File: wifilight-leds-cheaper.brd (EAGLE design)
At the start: 50.8 x 50.8 mm, 57 parts

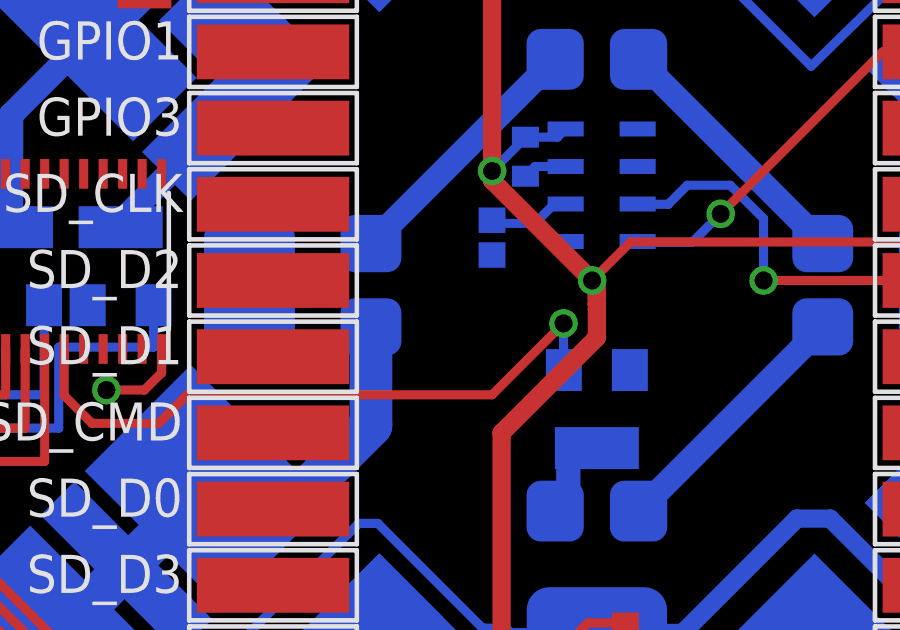
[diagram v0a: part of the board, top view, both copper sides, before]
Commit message: Damnit, how was I supposed to power this thing?
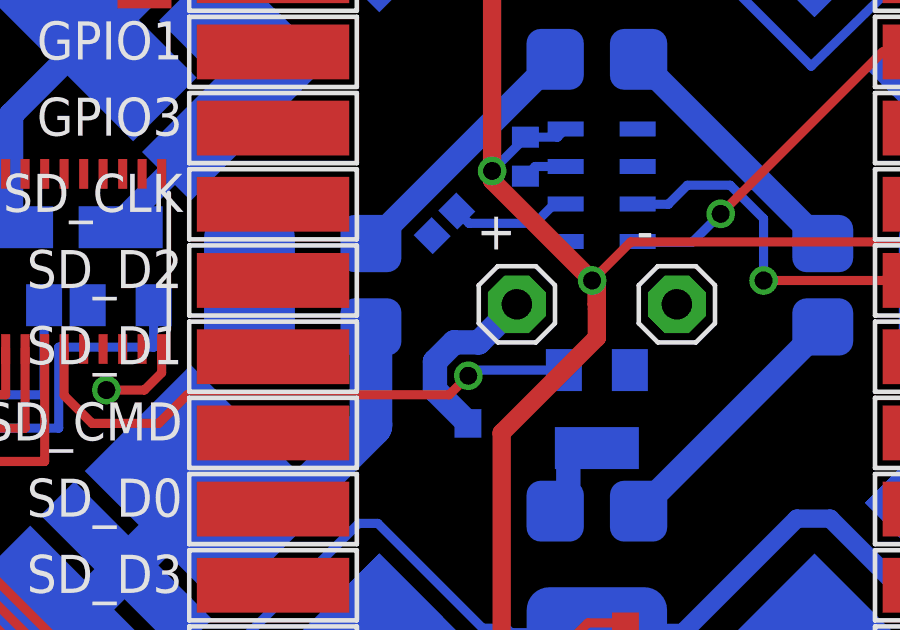
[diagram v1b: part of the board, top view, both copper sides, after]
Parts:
- added +, -: (no value), adafruit:1X01
- added D2: (no value), SparkFun-DiscreteSemi:SOD-123
- moved C4 1.66 mm to (20.3, 27.5), turned to 315 degrees
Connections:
- new net N$18: +.1, D2.A
- net 12V: now also D2.C
- net GND: now also -.1
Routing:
- net N$18: track 0.00 -> 6.04 mm
- net WHITE: track 21.5 -> 19.3 mm
- net N$17: track 2.76 -> 4.07 mm
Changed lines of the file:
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@@
 </element>
 <element name="TEMPERATURE" library="SparkFun-Sensors" package="LGA8" value="MPL3115A2LGA8" x="25.55875" y="28.73375" rot="MR180"/>
-<element name="C4" library="SparkFun-Capacitors" package="0402-CAP" value="0.1uF" x="21.9075" y="26.9875" rot="MR270">
-<attribute name="PROD_ID" value="CAP-12416" x="21.9075" y="26.9875" size="1.778" layer="28" rot="MR270" display="off"/>
+<element name="C4" library="SparkFun-Capacitors" package="0402-CAP" value="0.1uF" x="20.32" y="27.46375" rot="MR315">
+<attribute name="PROD_ID" value="CAP-12416" x="20.32" y="27.46375" size="1.778" layer="28" rot="MR315" display="off"/>
 </element>
 <element name="RESET" library="switch-omron" package="B3F-10XX" value="" x="25.4" y="45.212" rot="R270">
@@
 <element name="THINKING" library="led" package="CHIP-LED0805" value="" x="42.38625" y="42.545" rot="R45"/>
 <element name="R7" library="SparkFun-Passives" package="0402-RES" value="???" x="41.91" y="36.35375" rot="R90"/>
+<element name="+" library="adafruit" package="1X01" value="" x="22.733" y="24.765"/>
+<element name="-" library="adafruit" package="1X01" value="" x="28.067" y="24.765"/>
+<element name="D2" library="SparkFun-DiscreteSemi" package="SOD-123" value="" x="19.52625" y="20.79625" rot="MR180"/>
 </elements>
 <signals>
@@
 <wire x1="28.41625" y1="36.83" x2="25.55" y2="36.83" width="0.3048" layer="16"/>
 <wire x1="25.55" y1="36.83" x2="25.4" y2="36.98" width="0.3048" layer="16"/>
+<contactref element="-" pad="1"/>
 </signal>
 <signal name="SCL">
@@
 <wire x1="8.5725" y1="20.79625" x2="10.795" y2="20.79625" width="0.3048" layer="1"/>
 <wire x1="10.795" y1="20.79625" x2="11.7475" y2="21.74875" width="0.3048" layer="1"/>
-<wire x1="11.7475" y1="21.74875" x2="21.9075" y2="21.74875" width="0.3048" layer="1"/>
-<wire x1="21.9075" y1="21.74875" x2="24.28875" y2="24.13" width="0.3048" layer="1"/>
-<via x="24.28875" y="24.13" extent="1-16" drill="0.6"/>
-<wire x1="24.28875" y1="24.13" x2="24.28875" y2="22.58375" width="0.3048" layer="16"/>
+<wire x1="11.7475" y1="21.74875" x2="20.47875" y2="21.74875" width="0.3048" layer="1"/>
 <wire x1="24.28875" y1="22.58375" x2="24.3" y2="22.5725" width="0.3048" layer="16"/>
+<wire x1="24.3" y1="22.5725" x2="21.3025" y2="22.5725" width="0.3048" layer="16"/>
+<wire x1="21.3025" y1="22.5725" x2="21.11375" y2="22.38375" width="0.3048" layer="16"/>
+<via x="21.11375" y="22.38375" extent="1-16" drill="0.6"/>
+<wire x1="21.11375" y1="22.38375" x2="20.47875" y2="21.74875" width="0.3048" layer="1"/>
 </signal>
 <signal name="P_RED">
@@
 <wire x1="4.1275" y1="16.8275" x2="7.04039375" y2="13.91460625" width="0.3048" layer="16"/>
 <wire x1="7.04039375" y1="13.91460625" x2="7.04039375" y2="13.32289375" width="0.3048" layer="16"/>
+<contactref element="D2" pad="C"/>
+<wire x1="17.87" y1="20.7275" x2="17.95125" y2="20.79625" width="0" layer="19" extent="16-16"/>
 </signal>
 <signal name="N$10">
@@
 <wire x1="24.35875" y1="28.10875" x2="23.98125" y2="28.10875" width="0.3048" layer="16"/>
 <wire x1="23.98125" y1="28.10875" x2="23.33625" y2="27.46375" width="0.3048" layer="16"/>
-<wire x1="23.33625" y1="27.46375" x2="22.01125" y2="27.46375" width="0.3048" layer="16"/>
-<wire x1="22.01125" y1="27.46375" x2="21.9075" y2="27.5675" width="0.3048" layer="16"/>
+<wire x1="23.33625" y1="27.46375" x2="21.140246875" y2="27.46375" width="0.3048" layer="16"/>
+<wire x1="21.140246875" y1="27.46375" x2="20.730125" y2="27.873871875" width="0.3048" layer="16"/>
 </signal>
 <signal name="RESET">
@@
 <wire x1="41.895" y1="35.71875" x2="41.91" y2="35.70375" width="0.3048" layer="1"/>
 </signal>
+<signal name="N$18">
+<contactref element="D2" pad="A"/>
+<contactref element="+" pad="1"/>
+<wire x1="21.10125" y1="20.79625" x2="21.10125" y2="20.80875" width="0.8128" layer="16"/>
+<wire x1="21.10125" y1="20.80875" x2="20.0025" y2="21.9075" width="0.8128" layer="16"/>
+<wire x1="20.0025" y1="21.9075" x2="20.0025" y2="22.86" width="0.8128" layer="16"/>
+<wire x1="20.0025" y1="22.86" x2="20.6375" y2="23.495" width="0.8128" layer="16"/>
+<wire x1="20.6375" y1="23.495" x2="21.463" y2="23.495" width="0.8128" layer="16"/>
+<wire x1="21.463" y1="23.495" x2="22.733" y2="24.765" width="0.8128" layer="16"/>
+</signal>
 </signals>

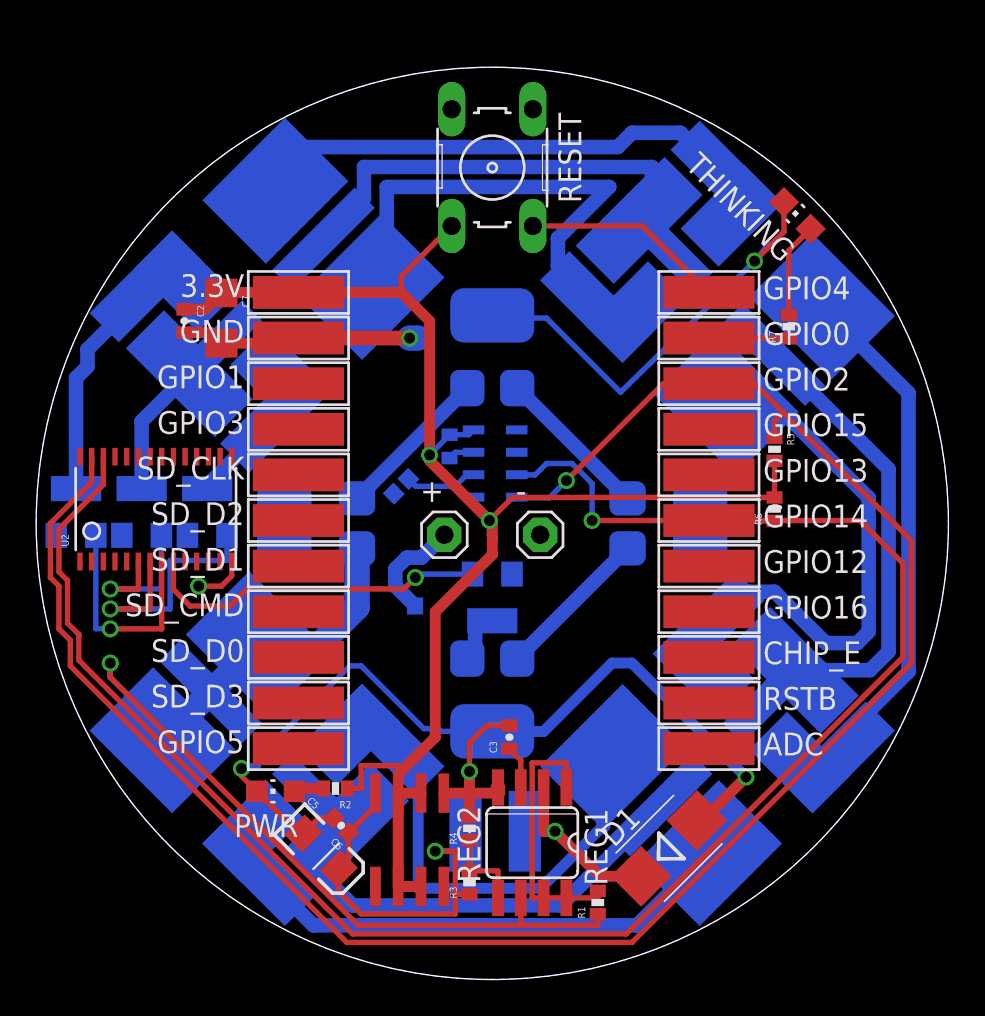
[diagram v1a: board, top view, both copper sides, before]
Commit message: As ordered recently. Discovered that SOT-23's are puny and 4 Luxeon Rebels are overkill. And that Banggood has cheaper ESP8266 modules.
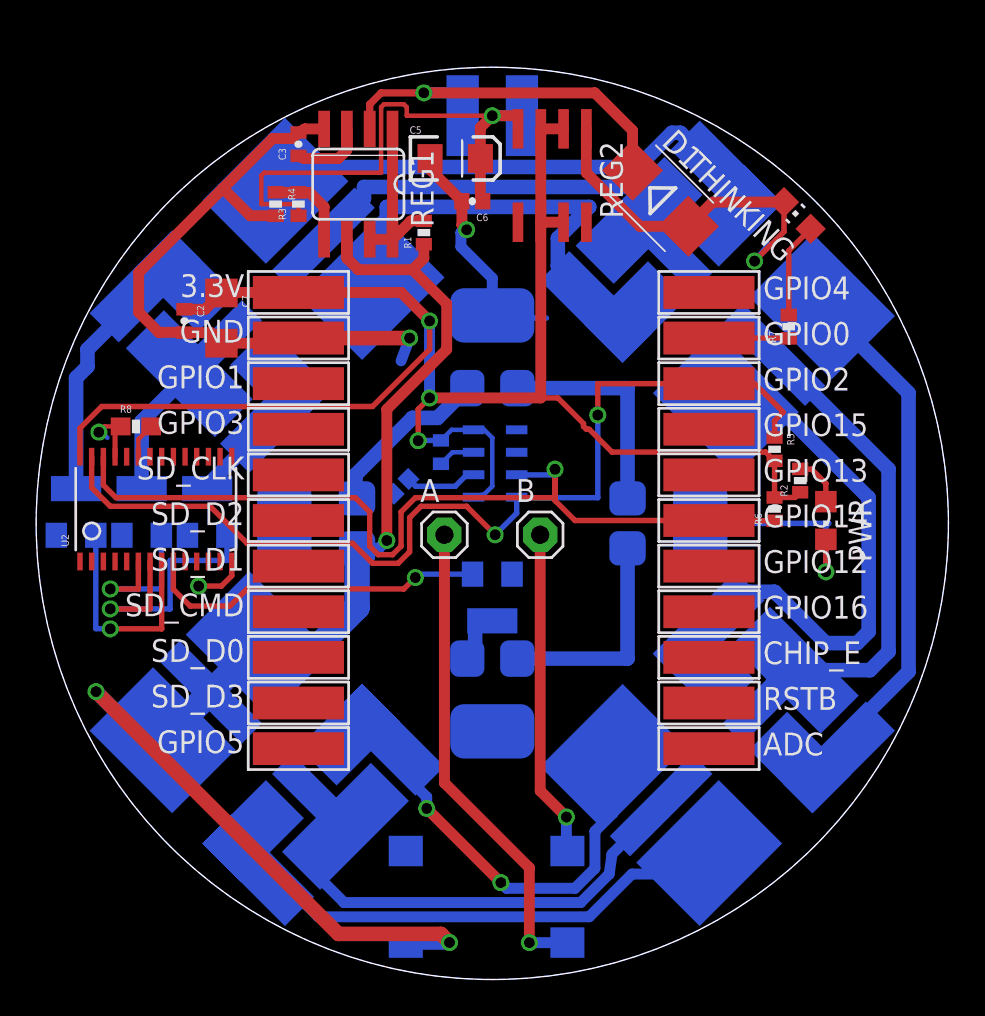
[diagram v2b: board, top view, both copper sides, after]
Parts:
- removed D2: (no value), SparkFun-DiscreteSemi:SOD-123
- removed RESET: (no value), switch-omron:B3F-10XX
- added B2: DBLS203G, rectifier:DBS
- added R8: 10K, SparkFun-Resistors:0603-RES
- Q3, Q4, Q5, Q6: value (none) -> FDN335N
- R5, R6: value (none) -> 1k
- U2: value (none) -> PCA9685
- moved L1 39.8 mm to (25.4, 48.1), turned to 0 degrees
- moved C5 39.3 mm to (23.3, 45.7), turned to 0 degrees
- moved R3 39.0 mm to (14.6, 43.2)
- moved R1 38.5 mm to (21.6, 41.6)
- moved REG1 37.9 mm to (17.9, 44.3)
- moved REG2 37.8 mm to (28.7, 44.8)
- moved R4 36.4 mm to (13.3, 43.2), turned to 270 degrees
- moved D1 36.2 mm to (34.8, 43.5), turned to 315 degrees
- moved C6 35.5 mm to (24.3, 43.3), turned to 180 degrees
- moved C3 35.0 mm to (14.6, 46.5)
- moved PWR 34.1 mm to (44.0, 25.6), turned to 180 degrees
- moved R2 31.0 mm to (42.5, 27.8), turned to 90 degrees
- moved C1 0.57 mm to (22.5, 29.4)
- renumbered + to A, - to B
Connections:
- removed net VDD: U2.28
- new net N$19: B.1, B2.AC2
- new net N$20: R8.2, U2.23
- net 12V: now also B2.+; no longer D2.C
- net 3.3V: now also U2.28; no longer RESET.4
- net GND: now also B2.-, R8.1, U2.25; no longer B.1
- net N$18: now also B2.AC1; no longer D2.A
- net RESET: no longer RESET.2
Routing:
- net SCL: track 105.6 -> 50.4 mm
- net SDA: track 109.4 -> 55.1 mm, vias 1 -> 2
- net N$18: track 6.04 -> 26.8 mm, vias 0 -> 1
- net N$19: track 0.00 -> 18.3 mm, vias 0 -> 1
- net 12V: track 60.3 -> 77.6 mm, vias 1 -> 3
- net SWE: track 10.6 -> 22.7 mm
- net RESET: track 11.3 -> 0.00 mm
- net 3.3V: track 86.1 -> 96.5 mm, vias 2 -> 3
- net 5V: track 21.5 -> 30.4 mm
- net GND: track 100.1 -> 92.9 mm
- net N$13: track 14.8 -> 9.38 mm
- net N$9: track 27.0 -> 23.2 mm
- net N$12: track 8.68 -> 12.3 mm
- net N$11: track 8.68 -> 12.3 mm
- net N$4: track 24.2 -> 22.0 mm
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
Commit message: Mk2
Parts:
- removed 3.3V, ADC, CHIP_E, GND, GPIO0, GPIO1, GPIO12, GPIO13, GPIO14, GPIO15, GPIO16, GPIO2, GPIO3, GPIO4, GPIO5, RSTB, SD_CLK, SD_CMD, SD_D0, SD_D1, SD_D2, SD_D3: WIREPADSMD5-1,8, wirepad:5-1,8
- removed LED4: OVSTRGBBCR8, led:OVSTRGBBCR8
- removed Q5, Q6: FDN335N, adafruit:SOT23-W
- removed U$4: LUXEON-REBEL, SparkFun-LED:LUXEON-REBEL
- added MPU: ESP8266_ESP-12, ESP8266-ESP12:ESP8266-ESP12
- added Q1, Q2: BUK98180-100A, nxp_60:SOT223
- C1, C2, C3: device SparkFun-Passives:0402-CAP -> resistor:C0805K
- C4, C6: device SparkFun-Capacitors:0402-CAP -> resistor:C0805K
- C7: device SparkFun-Capacitors:1206 -> resistor:C0805K
- Q3, Q4: value FDN335N -> BUK98180-100A; device adafruit:SOT23-W -> nxp_60:SOT223
- R1, R2, R3, R4, R5, R6, R7: device SparkFun-Passives:0402-RES -> resistor:R0805
- R8: device SparkFun-Resistors:0603-RES -> resistor:R0805
- moved D1 35.3 mm to (6.51, 22.4), turned to 90 degrees
- moved LED3 32.5 mm to (25.4, 7.94), turned to 0 degrees
- moved L1 32.5 mm to (8.10, 20.6)
- moved R8 32.0 mm to (37.5, 28.7), turned to 270 degrees
- moved R2 31.9 mm to (17.1, 47.1), flipped to the bottom, turned to 180 degrees
- moved Q3 31.3 mm to (28.8, 4.76), flipped to the top, turned to 180 degrees
- moved C3 30.4 mm to (7.46, 17.0), turned to 270 degrees
- moved U$3 30.3 mm to (7.14, 14.8), turned to 240 degrees
- moved U$1 30.3 mm to (43.7, 14.8), turned to 120 degrees
- moved PWR 30.2 mm to (25.4, 49.4), turned to 270 degrees
- moved U2 30.0 mm to (36.5, 23.2)
- moved C2 29.5 mm to (37.5, 32.7), turned to 90 degrees
- moved C5 28.4 mm to (3.97, 24.9), flipped to the bottom, turned to 180 degrees
- moved R4 27.5 mm to (20.0, 16.5)
- moved REG1 25.9 mm to (12.7, 18.9), turned to 270 degrees
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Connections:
- removed net N$12: U$3.CATHODE, U$4.ANODE
- removed net N$3: LED3.4, LED3.4@1, LED4.1
- removed net N$4: LED3.5, LED3.5@1, LED4.2
- removed net N$9: LED3.6, LED3.6@1, LED4.3
- new net N$25: MPU.13
- new net N$26: MPU.12
- new net N$27: MPU.11
- new net N$28: MPU.10
- new net N$29: MPU.9
- new net N$32: MPU.6
- new net N$33: MPU.4
- new net N$34: MPU.3
- new net N$35: MPU.2
- new net N$36: MPU.5
- net 3.3V: now also MPU.16; no longer 3.3V.1
- net BLUE: now also Q2.1; no longer Q5.1
- net GND: now also MPU.1, Q1.3, Q2.3, Q3.3, Q4.3; no longer GND.1, Q3.2, Q4.2, Q5.2, Q6.2, U$4.P$3
- net GREEN: now also Q4.1, U2.9; no longer Q6.1, U2.8
- net P_BLUE: now also LED3.6, LED3.6@1, Q2.2, Q2.4; no longer LED4.6, LED4.6@1, Q5.3
- net P_GREEN: now also LED3.4, LED3.4@1, Q4.2, Q4.4; no longer LED4.4, LED4.4@1, Q6.3
- net P_RED: now also LED3.5, LED3.5@1, Q3.2, Q3.4; no longer LED4.5, LED4.5@1, Q3.3
- net P_WHITE: now also Q1.2, Q1.4, U$3.CATHODE; no longer Q4.3, U$4.CATHODE
- net RED: now also U2.8; no longer U2.6
- net RESET: now also MPU.8; no longer GPIO4.1
- net SCL: now also MPU.15; no longer GPIO14.1
- net SDA: now also MPU.14; no longer GPIO2.1
- net THINKING: now also MPU.7; no longer GPIO0.1
- net WHITE: now also Q1.1, U2.6; no longer Q4.1, U2.9
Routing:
- net SDA: track 55.1 -> 18.3 mm
- net GND: track 92.9 -> 129.0 mm, vias 6 -> 10
- net 12V: track 77.6 -> 110.6 mm, vias 3 -> 6
- net N$10: track 9.60 -> 41.5 mm, vias 0 -> 2
- net SCL: track 50.4 -> 20.7 mm, vias 1 -> 2
- net N$11: track 12.3 -> 41.7 mm, vias 0 -> 2
- net N$3: track 28.7 -> 0.00 mm
- net N$18: track 26.8 -> 2.60 mm, vias 1 -> 0
- net N$9: track 23.2 -> 0.00 mm
- net N$4: track 22.0 -> 0.00 mm
- net P_GREEN: track 12.9 -> 34.1 mm, vias 0 -> 3
- net THINKING: track 4.45 -> 25.1 mm
- net N$19: track 18.3 -> 2.60 mm, vias 1 -> 0
- net P_WHITE: track 3.28 -> 18.8 mm, vias 0 -> 1
- net P_RED: track 7.50 -> 21.2 mm, vias 0 -> 1
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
